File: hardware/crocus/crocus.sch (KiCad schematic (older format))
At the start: 49 parts, among them J1 NEIGHBOR1, J2 NEIGHBOR2, J7 BONUS_ROW, P1 RP-SMA, P2 EXPANSION, T1 BALUN, U1 nRF24L01+, U2 PCA9674, Y1 XTAL

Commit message: crocus: finished layout
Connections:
- net GND: no longer J2.1 (P1)
- net AD0: now reaches R5.1, U2.1 (AD0), W12.2, W3.2, W6.2, W9.2
- net AD1: now reaches R4.1, U2.2 (AD1), W11.2, W2.2, W5.2, W8.2
- net AD2: now reaches R3.1, U2.3 (AD2), W1.2, W10.2, W4.2, W7.2
- net VBUS: no longer names the net of J2.2 (P2)
- no-connect marks 81 -> 83
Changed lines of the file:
@@
 $Comp
 L GND #PWR01
-U 1 1 55EACE84
-P 8950 2100
-F 0 "#PWR01" H 8950 1850 50  0001 C CNN
-F 1 "GND" H 8950 1950 50  0000 C CNN
-F 2 "" H 8950 2100 60  0000 C CNN
-F 3 "" H 8950 2100 60  0000 C CNN
-	1    8950 2100
-	0    1    1    0
-$EndComp
-$Comp
-L GND #PWR02
 U 1 1 55EAECD0
 P 8950 4700
-F 0 "#PWR02" H 8950 4450 50  0001 C CNN
+F 0 "#PWR01" H 8950 4450 50  0001 C CNN
 F 1 "GND" H 8950 4550 50  0000 C CNN
 F 2 "" H 8950 4700 60  0000 C CNN
@@
 	0    1    1    0
 $EndComp
-Text Label 9850 2100 2    40   ~ 0
-VBUS
 $Comp
 L CONN_02X20 J1
@@
 $EndComp
 $Comp
-L GND #PWR03
+L GND #PWR02
 U 1 1 5600F9D3
 P 9500 1200
-F 0 "#PWR03" H 9500 950 50  0001 C CNN
+F 0 "#PWR02" H 9500 950 50  0001 C CNN
 F 1 "GND" H 9500 1050 50  0000 C CNN
 F 2 "" H 9500 1200 60  0000 C CNN
@@
 $EndComp
 $Comp
-L GND #PWR04
+L GND #PWR03
 U 1 1 560100F9
 P 10000 1350
-F 0 "#PWR04" H 10000 1100 50  0001 C CNN
+F 0 "#PWR03" H 10000 1100 50  0001 C CNN
 F 1 "GND" H 10000 1200 50  0000 C CNN
 F 2 "" H 10000 1350 60  0000 C CNN
@@
 $EndComp
 $Comp
-L GND #PWR05
+L GND #PWR04
 U 1 1 56010AE1
 P 8500 1200
-F 0 "#PWR05" H 8500 950 50  0001 C CNN
+F 0 "#PWR04" H 8500 950 50  0001 C CNN
 F 1 "GND" H 8500 1050 50  0000 C CNN
 F 2 "" H 8500 1200 60  0000 C CNN
@@
 $EndComp
 $Comp
-L GND #PWR06
+L GND #PWR05
 U 1 1 56010AEF
 P 9000 1350
-F 0 "#PWR06" H 9000 1100 50  0001 C CNN
+F 0 "#PWR05" H 9000 1100 50  0001 C CNN
 F 1 "GND" H 9000 1200 50  0000 C CNN
 F 2 "" H 9000 1350 60  0000 C CNN
@@
 $EndComp
 $Comp
-L GND #PWR07
+L GND #PWR06
 U 1 1 5604F191
 P 8400 4350
-F 0 "#PWR07" H 8400 4100 50  0001 C CNN
+F 0 "#PWR06" H 8400 4100 50  0001 C CNN
 F 1 "GND" H 8400 4200 50  0000 C CNN
 F 2 "" H 8400 4350 60  0000 C CNN
@@
 $EndComp
 $Comp
-L GND #PWR08
+L GND #PWR07
 U 1 1 5604F268
 P 5850 4450
-F 0 "#PWR08" H 5850 4200 50  0001 C CNN
+F 0 "#PWR07" H 5850 4200 50  0001 C CNN
 F 1 "GND" H 5850 4300 50  0000 C CNN
 F 2 "" H 5850 4450 60  0000 C CNN
@@
 $EndComp
 $Comp
-L GND #PWR09
+L GND #PWR08
 U 1 1 5604F2B2
 P 5650 2900
-F 0 "#PWR09" H 5650 2650 50  0001 C CNN
+F 0 "#PWR08" H 5650 2650 50  0001 C CNN
 F 1 "GND" H 5650 2750 50  0000 C CNN
 F 2 "" H 5650 2900 60  0000 C CNN
@@
 $EndComp
 $Comp
-L GND #PWR010
+L GND #PWR09
 U 1 1 5604F2E1
 P 5950 2900
-F 0 "#PWR010" H 5950 2650 50  0001 C CNN
+F 0 "#PWR09" H 5950 2650 50  0001 C CNN
 F 1 "GND" H 5950 2750 50  0000 C CNN
 F 2 "" H 5950 2900 60  0000 C CNN
@@
 $EndComp
 $Comp
-L GND #PWR011
+L GND #PWR010
 U 1 1 5604F307
 P 6600 3550
-F 0 "#PWR011" H 6600 3300 50  0001 C CNN
+F 0 "#PWR010" H 6600 3300 50  0001 C CNN
 F 1 "GND" H 6600 3400 50  0000 C CNN
 F 2 "" H 6600 3550 60  0000 C CNN
@@
 $EndComp
 $Comp
-L VCC #PWR012
+L VCC #PWR011
 U 1 1 5604F59C
 P 5850 2750
-F 0 "#PWR012" H 5850 2600 50  0001 C CNN
+F 0 "#PWR011" H 5850 2600 50  0001 C CNN
 F 1 "VCC" H 5850 2900 50  0000 C CNN
 F 2 "" H 5850 2750 60  0000 C CNN
@@
 $EndComp
 $Comp
-L VCC #PWR013
+L VCC #PWR012
 U 1 1 5604F5F8
 P 6750 3450
-F 0 "#PWR013" H 6750 3300 50  0001 C CNN
+F 0 "#PWR012" H 6750 3300 50  0001 C CNN
 F 1 "VCC" H 6750 3600 50  0000 C CNN
 F 2 "" H 6750 3450 60  0000 C CNN
@@
 $EndComp
 $Comp
-L VCC #PWR014
+L VCC #PWR013
 U 1 1 5604F65B
 P 5750 4600
-F 0 "#PWR014" H 5750 4450 50  0001 C CNN
+F 0 "#PWR013" H 5750 4450 50  0001 C CNN
 F 1 "VCC" H 5750 4750 50  0000 C CNN
 F 2 "" H 5750 4600 60  0000 C CNN
@@
 $EndComp
 $Comp
-L GND #PWR015
+L GND #PWR014
 U 1 1 5605045B
 P 5950 5300
-F 0 "#PWR015" H 5950 5050 50  0001 C CNN
+F 0 "#PWR014" H 5950 5050 50  0001 C CNN
 F 1 "GND" H 5950 5150 50  0000 C CNN
 F 2 "" H 5950 5300 60  0000 C CNN
@@
 $EndComp
 $Comp
-L GND #PWR016
+L GND #PWR015
 U 1 1 5605049D
 P 6450 5300
-F 0 "#PWR016" H 6450 5050 50  0001 C CNN
+F 0 "#PWR015" H 6450 5050 50  0001 C CNN
 F 1 "GND" H 6450 5150 50  0000 C CNN
 F 2 "" H 6450 5300 60  0000 C CNN
@@
 $EndComp
 $Comp
-L GND #PWR017
+L GND #PWR016
 U 1 1 56051138
 P 6050 2050
-F 0 "#PWR017" H 6050 1800 50  0001 C CNN
+F 0 "#PWR016" H 6050 1800 50  0001 C CNN
 F 1 "GND" H 6050 1900 50  0000 C CNN
 F 2 "" H 6050 2050 60  0000 C CNN
@@
 $EndComp
 $Comp
-L GND #PWR018
+L GND #PWR017
 U 1 1 56052DB2
 P 8150 3650
-F 0 "#PWR018" H 8150 3400 50  0001 C CNN
+F 0 "#PWR017" H 8150 3400 50  0001 C CNN
 F 1 "GND" H 8150 3500 50  0000 C CNN
 F 2 "" H 8150 3650 60  0000 C CNN
@@
 $EndComp
 $Comp
-L GND #PWR019
+L GND #PWR018
 U 1 1 56053B17
 P 6850 4350
-F 0 "#PWR019" H 6850 4100 50  0001 C CNN
+F 0 "#PWR018" H 6850 4100 50  0001 C CNN
 F 1 "GND" H 6850 4200 50  0000 C CNN
 F 2 "" H 6850 4350 60  0000 C CNN
@@
 $EndComp
 $Comp
-L GND #PWR020
+L GND #PWR019
 U 1 1 56054D2F
 P 5150 2950
-F 0 "#PWR020" H 5150 2700 50  0001 C CNN
+F 0 "#PWR019" H 5150 2700 50  0001 C CNN
 F 1 "GND" H 5150 2800 50  0000 C CNN
 F 2 "" H 5150 2950 60  0000 C CNN
@@
 $EndComp
 $Comp
-L VCC #PWR021
+L VCC #PWR020
 U 1 1 5605549D
 P 7650 5600
-F 0 "#PWR021" H 7650 5450 50  0001 C CNN
+F 0 "#PWR020" H 7650 5450 50  0001 C CNN
 F 1 "VCC" H 7650 5750 50  0000 C CNN
 F 2 "" H 7650 5600 60  0000 C CNN
@@
 $EndComp
 $Comp
-L GND #PWR022
+L GND #PWR021
 U 1 1 560556B9
 P 7650 6300
-F 0 "#PWR022" H 7650 6050 50  0001 C CNN
+F 0 "#PWR021" H 7650 6050 50  0001 C CNN
 F 1 "GND" H 7650 6150 50  0000 C CNN
 F 2 "" H 7650 6300 60  0000 C CNN
@@
 $EndComp
 $Comp
-L GND #PWR023
+L GND #PWR022
 U 1 1 5605B1C2
 P 2500 3850
-F 0 "#PWR023" H 2500 3600 50  0001 C CNN
+F 0 "#PWR022" H 2500 3600 50  0001 C CNN
 F 1 "GND" H 2500 3700 50  0000 C CNN
 F 2 "" H 2500 3850 60  0000 C CNN
@@
 $EndComp
 $Comp
-L VCC #PWR024
+L VCC #PWR023
 U 1 1 5605B330
 P 3800 2200
-F 0 "#PWR024" H 3800 2050 50  0001 C CNN
+F 0 "#PWR023" H 3800 2050 50  0001 C CNN
 F 1 "VCC" H 3800 2350 50  0000 C CNN
 F 2 "" H 3800 2200 60  0000 C CNN
@@
 INT
 $Comp
-L VCC #PWR025
+L VCC #PWR024
 U 1 1 5605BD4D
 P 4100 2850
-F 0 "#PWR025" H 4100 2700 50  0001 C CNN
+F 0 "#PWR024" H 4100 2700 50  0001 C CNN
 F 1 "VCC" H 4100 3000 50  0000 C CNN
 F 2 "" H 4100 2850 60  0000 C CNN
@@
 $EndComp
 $Comp
-L GND #PWR026
+L GND #PWR025
 U 1 1 5605C3C4
 P 2100 7450
-F 0 "#PWR026" H 2100 7200 50  0001 C CNN
+F 0 "#PWR025" H 2100 7200 50  0001 C CNN
 F 1 "GND" H 2100 7300 50  0000 C CNN
 F 2 "" H 2100 7450 60  0000 C CNN
@@
 $EndComp
 $Comp
-L VCC #PWR027
+L VCC #PWR026
 U 1 1 5605C8C7
 P 2800 6750
-F 0 "#PWR027" H 2800 6600 50  0001 C CNN
+F 0 "#PWR026" H 2800 6600 50  0001 C CNN
 F 1 "VCC" H 2800 6900 50  0000 C CNN
 F 2 "" H 2800 6750 60  0000 C CNN
@@
 CE
 $Comp
-L GND #PWR028
+L GND #PWR027
 U 1 1 5605EBAA
 P 3800 2800
-F 0 "#PWR028" H 3800 2550 50  0001 C CNN
+F 0 "#PWR027" H 3800 2550 50  0001 C CNN
 F 1 "GND" H 3800 2650 50  0000 C CNN
 F 2 "" H 3800 2800 60  0000 C CNN
@@
 RF
 $Comp
-L GND #PWR029
+L GND #PWR028
 U 1 1 56062798
 P 3100 2600
-F 0 "#PWR029" H 3100 2350 50  0001 C CNN
+F 0 "#PWR028" H 3100 2350 50  0001 C CNN
 F 1 "GND" H 3100 2450 50  0000 C CNN
 F 2 "" H 3100 2600 60  0000 C CNN
@@
 $EndComp
 $Comp
-L VCC #PWR030
+L VCC #PWR029
 U 1 1 56062D36
 P 3100 1800
-F 0 "#PWR030" H 3100 1650 50  0001 C CNN
+F 0 "#PWR029" H 3100 1650 50  0001 C CNN
 F 1 "VCC" H 3100 1950 50  0000 C CNN
 F 2 "" H 3100 1800 60  0000 C CNN
@@
 	8850 6100 9150 6100
 Wire Wire Line
-	8950 2100 9150 2100
-Wire Wire Line
-	9850 2100 9650 2100
-Wire Wire Line
 	9650 4700 9850 4700
 Wire Wire Line
@@
 Connection ~ 1750 2500
 $Comp
-L GND #PWR031
+L GND #PWR030
 U 1 1 5606333D
 P 2350 2600
-F 0 "#PWR031" H 2350 2350 50  0001 C CNN
+F 0 "#PWR030" H 2350 2350 50  0001 C CNN
 F 1 "GND" H 2350 2450 50  0000 C CNN
 F 2 "" H 2350 2600 60  0000 C CNN
@@
 	2350 2500 2350 2600
 $Comp
-L VCC #PWR032
+L VCC #PWR031
 U 1 1 56063346
 P 2350 1800
-F 0 "#PWR032" H 2350 1650 50  0001 C CNN
+F 0 "#PWR031" H 2350 1650 50  0001 C CNN
 F 1 "VCC" H 2350 1950 50  0000 C CNN
 F 2 "" H 2350 1800 60  0000 C CNN
@@
 Connection ~ 1000 2500
 $Comp
-L GND #PWR033
+L GND #PWR032
 U 1 1 56063AEC
 P 1600 2600
-F 0 "#PWR033" H 1600 2350 50  0001 C CNN
+F 0 "#PWR032" H 1600 2350 50  0001 C CNN
 F 1 "GND" H 1600 2450 50  0000 C CNN
 F 2 "" H 1600 2600 60  0000 C CNN
@@
 	1600 2500 1600 2600
 $Comp
-L VCC #PWR034
+L VCC #PWR033
 U 1 1 56063AF4
 P 1600 1800
-F 0 "#PWR034" H 1600 1650 50  0001 C CNN
+F 0 "#PWR033" H 1600 1650 50  0001 C CNN
 F 1 "VCC" H 1600 1950 50  0000 C CNN
 F 2 "" H 1600 1800 60  0000 C CNN
@@
 	1750 3750 1750 3650
 $Comp
-L GND #PWR035
+L GND #PWR034
 U 1 1 56066602
 P 2050 3750
-F 0 "#PWR035" H 2050 3500 50  0001 C CNN
+F 0 "#PWR034" H 2050 3500 50  0001 C CNN
 F 1 "GND" H 2050 3600 50  0000 C CNN
 F 2 "" H 2050 3750 60  0000 C CNN
@@
 $EndComp
 $Comp
-L GND #PWR036
+L GND #PWR035
 U 1 1 560666F5
 P 1000 3750
-F 0 "#PWR036" H 1000 3500 50  0001 C CNN
+F 0 "#PWR035" H 1000 3500 50  0001 C CNN
 F 1 "GND" H 1000 3600 50  0000 C CNN
 F 2 "" H 1000 3750 60  0000 C CNN
@@
 Default I2C address set by resistors:\n0x40 read\n0x41 write\n0x20 7 bit (without r/w bit)
 $Comp
-L GND #PWR037
+L GND #PWR036
 U 1 1 56067F1F
 P 1750 3750
-F 0 "#PWR037" H 1750 3500 50  0001 C CNN
+F 0 "#PWR036" H 1750 3500 50  0001 C CNN
 F 1 "GND" H 1750 3600 50  0000 C CNN
 F 2 "" H 1750 3750 60  0000 C CNN
@@
 P5_7
 $Comp
-L VCC #PWR038
+L VCC #PWR037
 U 1 1 55EAF03E
 P 9850 4700
-F 0 "#PWR038" H 9850 4550 50  0001 C CNN
+F 0 "#PWR037" H 9850 4550 50  0001 C CNN
 F 1 "VCC" H 9850 4850 50  0000 C CNN
 F 2 "" H 9850 4700 60  0000 C CNN
@@
 	-1   0    0    1
 $EndComp
+Text Label 2250 3050 0    40   ~ 0
+AD0
+Text Label 2250 3150 0    40   ~ 0
+AD1
+Text Label 2250 3250 0    40   ~ 0
+AD2
+NoConn ~ 9650 2100
+NoConn ~ 9150 2100
 $EndSCHEMATC

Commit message: crocus: switched from vertical to PCB edge RP-SMA connector
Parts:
- P1: footprint gsg-modules:SMA-VERTICAL -> gsg-modules:SMA-EDGE
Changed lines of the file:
@@
 F 0 "P1" H 8410 4170 50  0000 C CNN
 F 1 "RP-SMA" V 8510 3990 50  0000 C CNN
-F 2 "gsg-modules:SMA-VERTICAL" H 8400 4050 60  0001 C CNN
+F 2 "gsg-modules:SMA-EDGE" H 8400 4050 60  0001 C CNN
 F 3 "" H 8400 4050 60  0000 C CNN
 	1    8400 4050

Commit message: neighbors: pin header part selection
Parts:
- J1, J2: Description (none) -> CONN RCPT .100\" 40POS DUAL-ROW STACKING GOLD; Manufacturer (none) -> Samtec; Part Number (none) -> SSQ-120-23-G-D
- J7: Description (none) -> CONN RCPT .100\" 20POS SINGLE-ROW STACKING GOLD; Manufacturer (none) -> Samtec; Part Number (none) -> SSQ-120-23-G-S
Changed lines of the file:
@@
 F 2 "gsg-modules:HEADER-2x20" H 9400 2100 60  0001 C CNN
 F 3 "" H 9400 2100 60  0000 C CNN
+F 4 "Samtec" H 9400 3050 60  0001 C CNN "Manufacturer"
+F 5 "SSQ-120-23-G-D" H 9400 3050 60  0001 C CNN "Part Number"
+F 6 "CONN RCPT .100\" 40POS DUAL-ROW STACKING GOLD" H 9400 3050 60  0001 C CNN "Description"
 	1    9400 3050
 	1    0    0    -1
@@
 F 2 "gsg-modules:HEADER-2x20" H 9400 4700 60  0001 C CNN
 F 3 "" H 9400 4700 60  0000 C CNN
+F 4 "Samtec" H 9400 5650 60  0001 C CNN "Manufacturer"
+F 5 "SSQ-120-23-G-D" H 9400 5650 60  0001 C CNN "Part Number"
+F 6 "CONN RCPT .100\" 40POS DUAL-ROW STACKING GOLD" H 9400 5650 60  0001 C CNN "Description"
 	1    9400 5650
 	1    0    0    -1
@@
 F 2 "gsg-modules:HEADER-1x20" H 5000 7500 60  0001 C CNN
 F 3 "" H 5000 7500 60  0000 C CNN
-F 4 "DNP" V 5200 7500 60  0000 C CNN "Note"
+F 4 "Samtec" H 5000 7500 60  0001 C CNN "Manufacturer"
+F 5 "SSQ-120-23-G-S" H 5000 7500 60  0001 C CNN "Part Number"
+F 6 "CONN RCPT .100\" 20POS SINGLE-ROW STACKING GOLD" H 5000 7500 60  0001 C CNN "Description"
+F 7 "DNP" V 5200 7500 60  0000 C CNN "Note"
 	1    5000 7500
 	0    -1   -1   0

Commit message: neighbors: alternate header selection
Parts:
- J1, J2: Note (none) -> Alternate: https://www.adafruit.com/products/2223
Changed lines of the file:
@@
 F 5 "SSQ-120-23-G-D" H 9400 3050 60  0001 C CNN "Part Number"
 F 6 "CONN RCPT .100\" 40POS DUAL-ROW STACKING GOLD" H 9400 3050 60  0001 C CNN "Description"
+F 7 "Alternate: https://www.adafruit.com/products/2223" H 9400 3050 60  0001 C CNN "Note"
 	1    9400 3050
 	1    0    0    -1
@@
 F 5 "SSQ-120-23-G-D" H 9400 5650 60  0001 C CNN "Part Number"
 F 6 "CONN RCPT .100\" 40POS DUAL-ROW STACKING GOLD" H 9400 5650 60  0001 C CNN "Description"
+F 7 "Alternate: https://www.adafruit.com/products/2223" H 9400 5650 60  0001 C CNN "Note"
 	1    9400 5650
 	1    0    0    -1

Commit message: crocus: added part number for P1
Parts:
- P1: Manufacturer (none) -> Linx Technologies; Part Number (none) -> CONREVSMA003.031
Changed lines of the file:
@@
 F 2 "gsg-modules:SMA-EDGE" H 8400 4050 60  0001 C CNN
 F 3 "" H 8400 4050 60  0000 C CNN
+F 4 "Linx Technologies" H 8400 4050 60  0001 C CNN "Manufacturer"
+F 5 "CONREVSMA003.031" H 8400 4050 60  0001 C CNN "Part Number"
 	1    8400 4050
 	1    0    0    -1

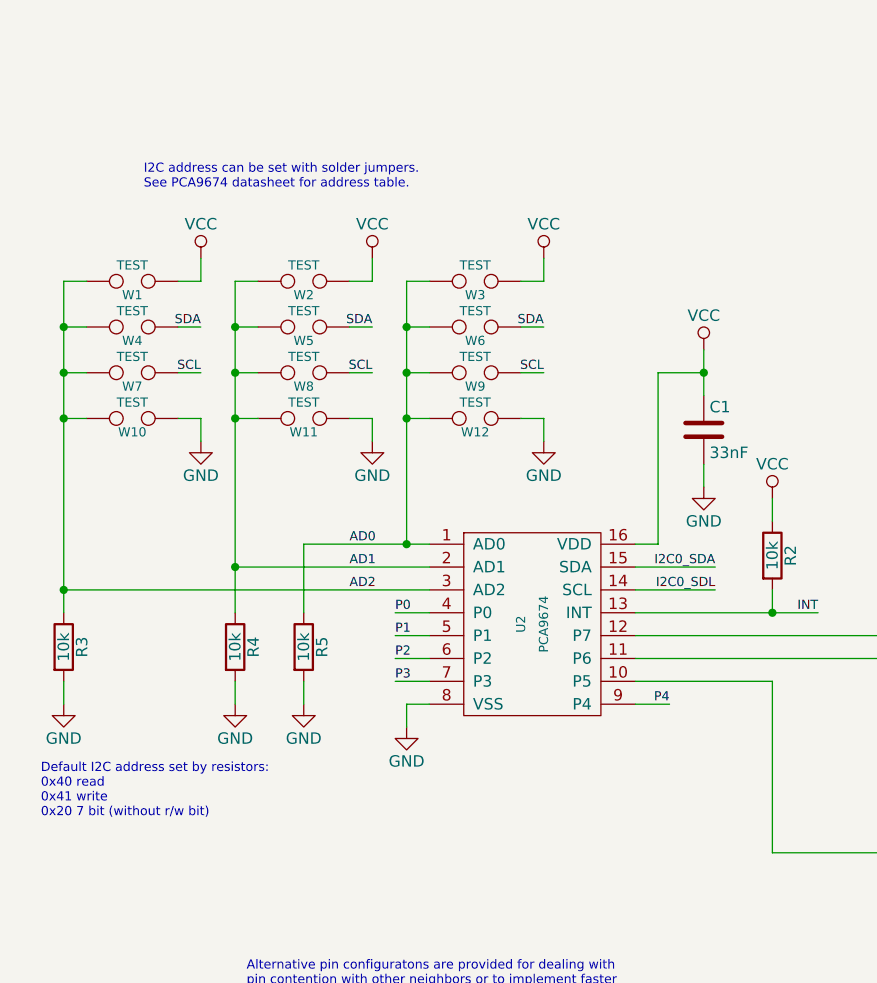
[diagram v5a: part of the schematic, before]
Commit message: Crocus: Corrected I2C connection errors, thanks to docprofsky!
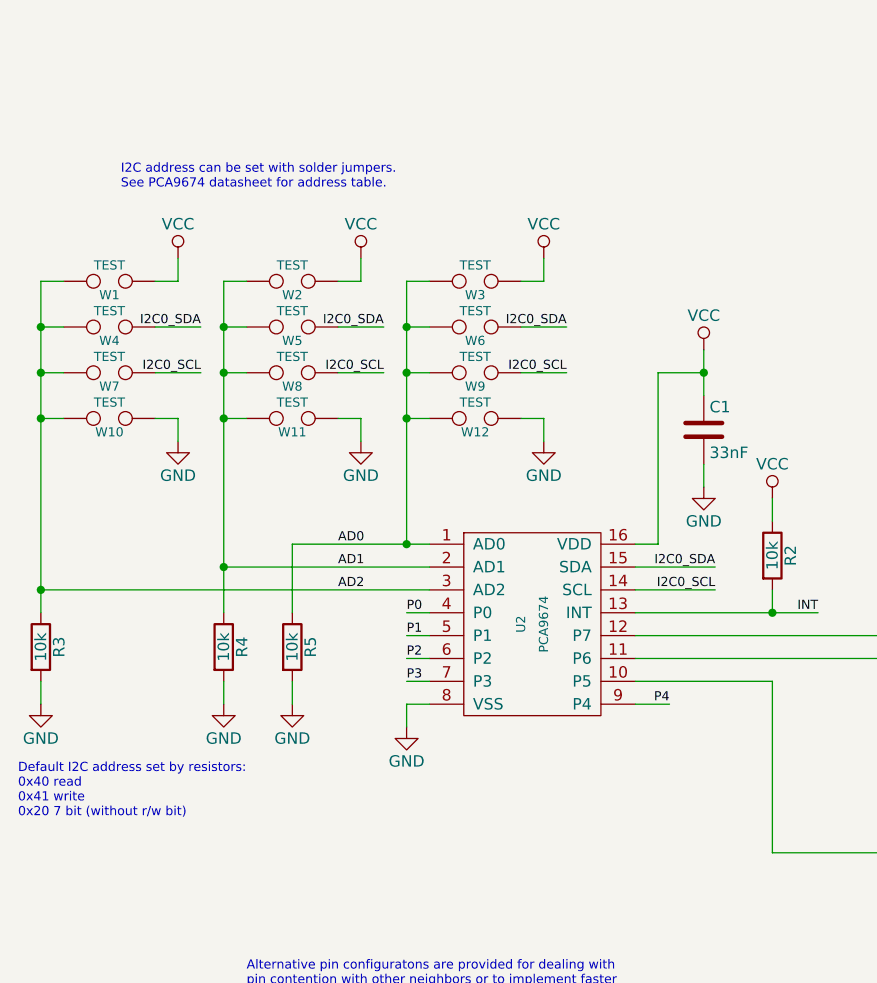
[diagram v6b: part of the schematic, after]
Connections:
- net I2C0_SDL is gone; now on net I2C0_SCL: U2.14 (SCL)
- net SCL is gone; now on net I2C0_SCL: W7.1, W8.1, W9.1
- net SDA is gone; now on net I2C0_SDA: W4.1, W5.1, W6.1
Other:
- moved on the sheet: R3, R4, R5, W1, W10, W11, W2, W4, W5, W7, W8
